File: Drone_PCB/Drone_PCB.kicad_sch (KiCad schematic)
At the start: 13 parts, among them U1 STM32F411RCT6

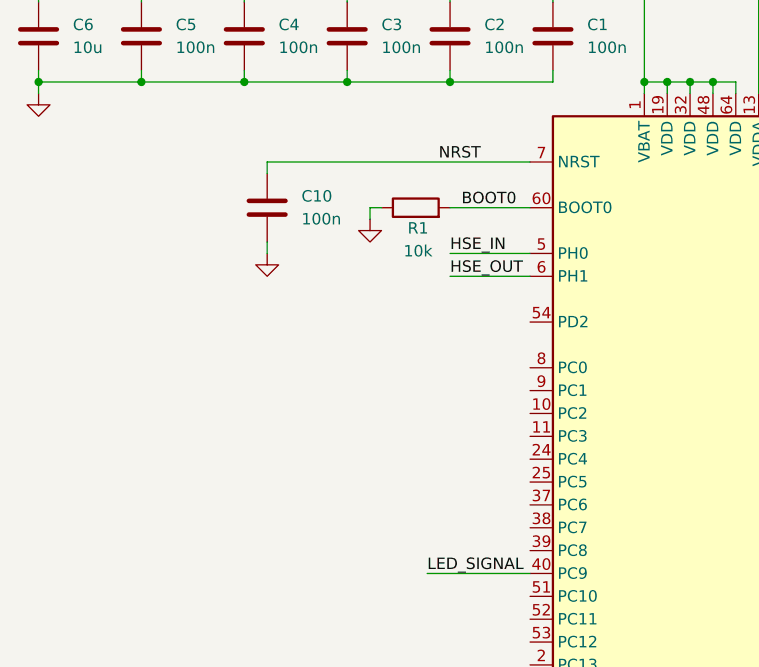
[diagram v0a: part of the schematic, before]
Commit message: Crystal Oscillator
I've decided to pick this one:
https://www.tme.eu/pl/details/26.00m-smdhc49s/rezonatory-kwarcowe-smd/yic/
It has 26MHz ( it's maximum input from STM Cube IDE ). It has 20pF, so to calculate two other capacitors we do this: 20pF - 5pF (that's maximum constant value)
15pF * 2 = 30pF each
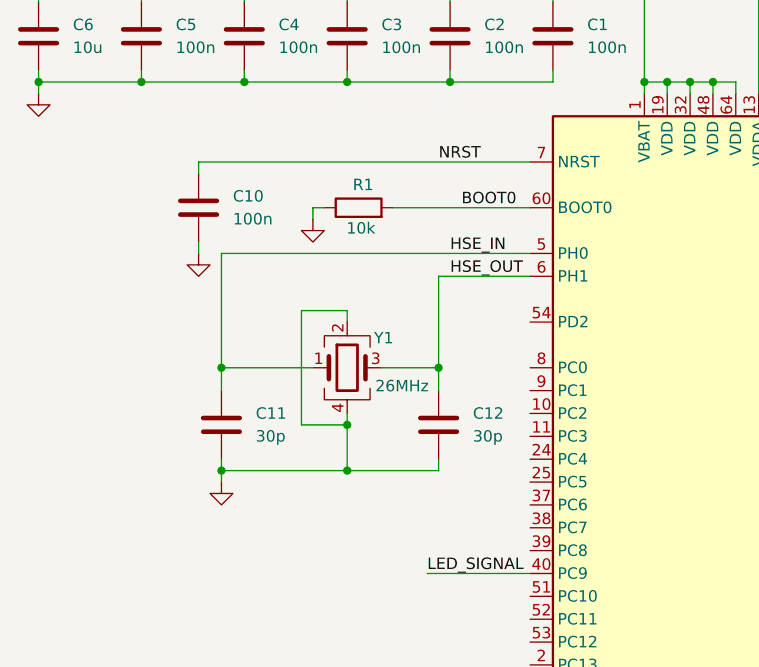
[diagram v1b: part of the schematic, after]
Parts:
- added C11, C12: 30p, symbol Device:C
- added Y1: 26MHz, symbol Device:Crystal_GND24
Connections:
- net GND: now also C11.2, C12.2, Y1.2, Y1.4
- net HSE_IN: now also C11.1, Y1.1
- net HSE_OUT: now also C12.1, Y1.3
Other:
- moved on the sheet: C10, R1

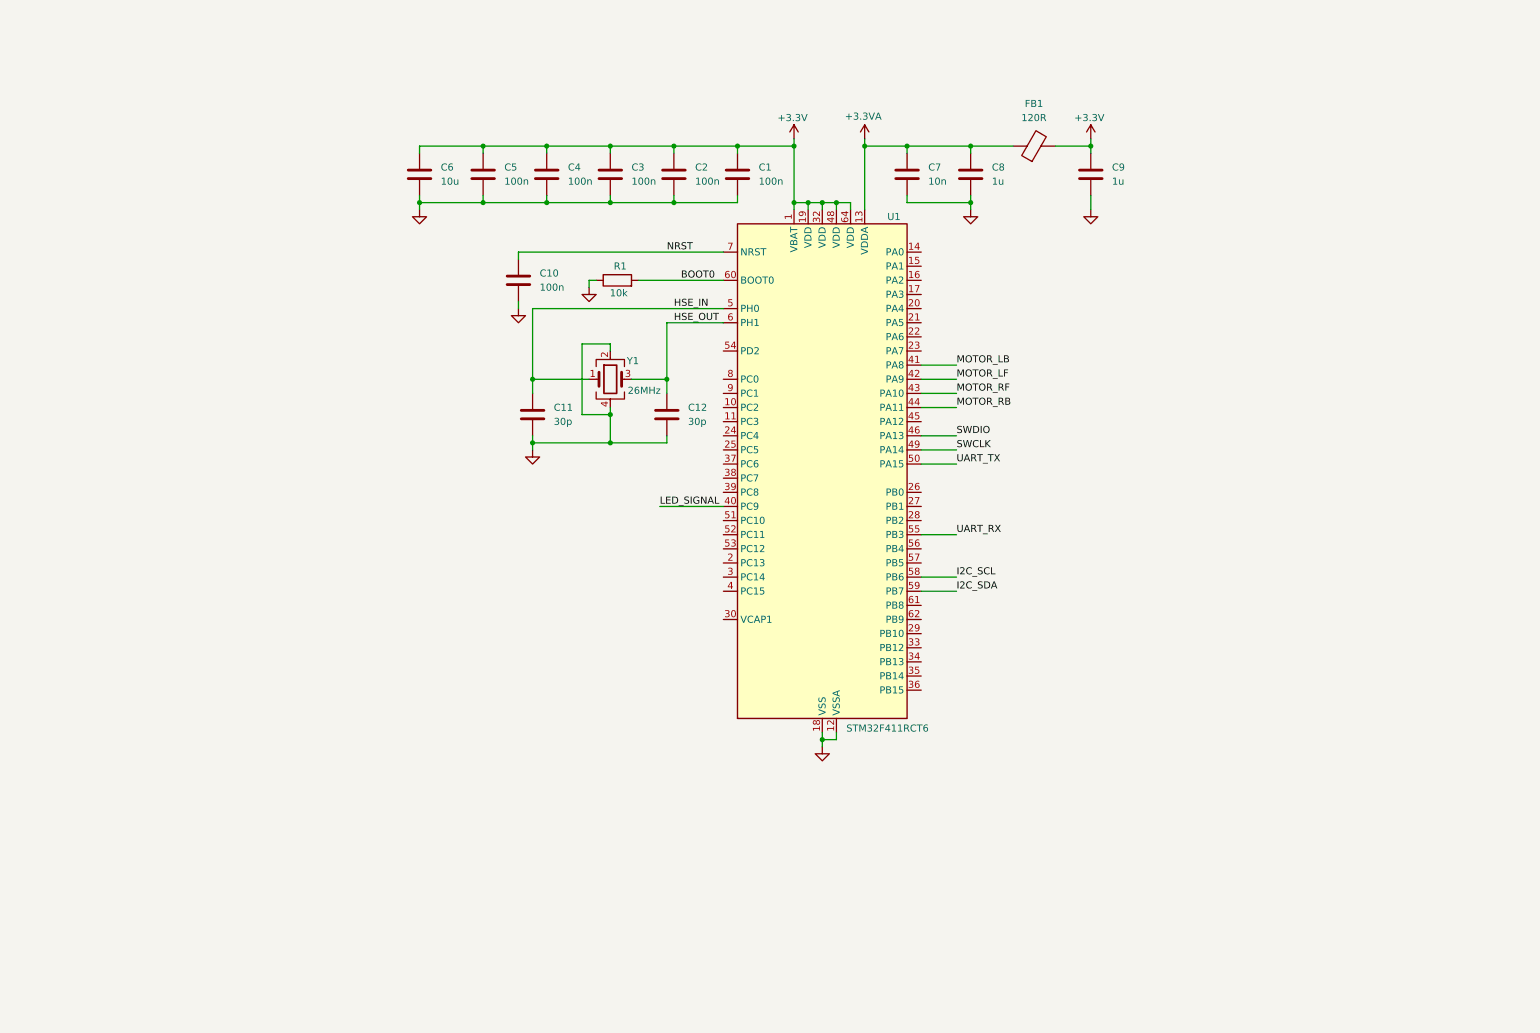
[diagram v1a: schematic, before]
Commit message: Voltage regulator + Outputs
I selected AP2112K as voltage regulator from 5/3.7V to 3.3V.
https://www.tme.eu/pl/details/ap2112k-3.3trg1/stabilizatory-napiecia-nieregulowane-ldo/diodes-incorporated/
In future I will add charging module
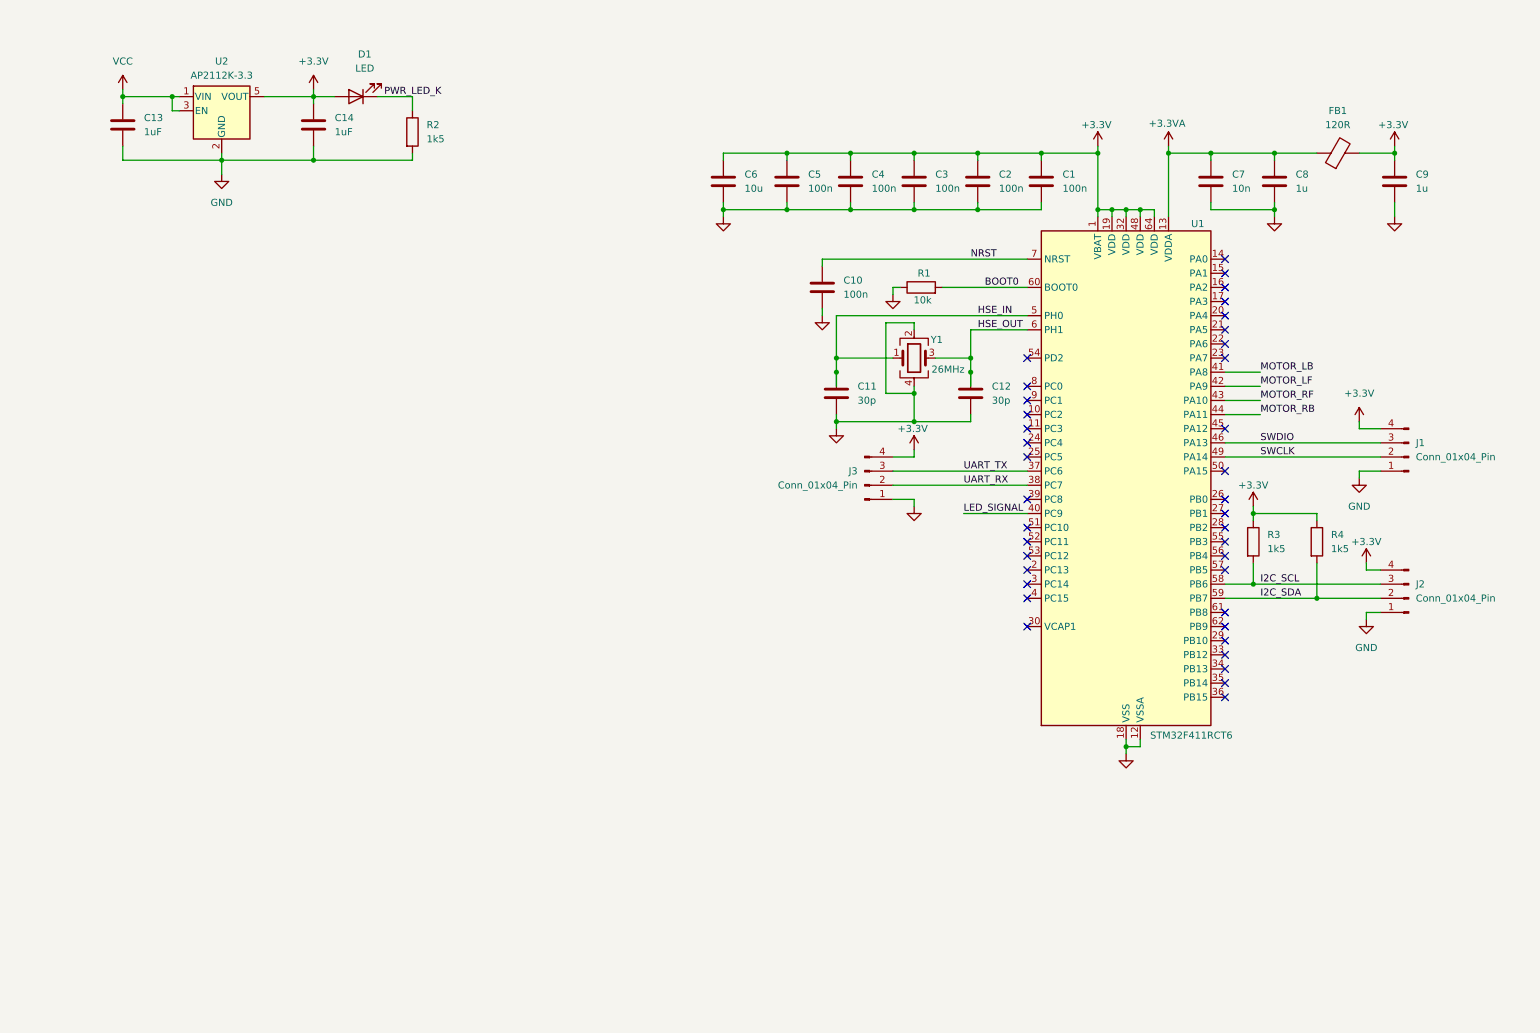
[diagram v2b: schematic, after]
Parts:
- added C13, C14: 1uF, symbol Device:C
- added D1: LED, symbol Device:LED
- added J1, J2, J3: Conn_01x04_Pin, symbol Connector:Conn_01x04_Pin
- added R2, R3, R4: 1k5, symbol Device:R
- added U2: AP2112K-3.3, Package_TO_SOT_SMD:SOT-23-5, symbol Regulator_Linear:AP2112K-3.3
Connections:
- net +3.3V: now also C14.1, D1.2 (A), J1.4 (Pin_4), J2.4 (Pin_4), J3.4 (Pin_4), R3.1, R4.1, U2.5 (VOUT)
- net GND: now also C13.2, C14.2, J1.1 (Pin_1), J2.1 (Pin_1), J3.1 (Pin_1), R2.2, U2.2 (GND)
- net I2C_SCL: now also J2.3 (Pin_3), R3.2
- net I2C_SDA: now also J2.2 (Pin_2), R4.2
- net SWCLK: now also J1.2 (Pin_2)
- net SWDIO: now also J1.3 (Pin_3)
- net UART_RX: now also U1.38 (PC7), J3.2 (Pin_2); no longer U1.55 (PB3)
- net UART_TX: now also U1.37 (PC6), J3.3 (Pin_3); no longer U1.50 (PA15)
- new net PWR_LED_K: D1.1 (K), R2.1
- new net VCC: C13.1, U2.1 (VIN), U2.3 (EN)
- no-connect marks 0 -> 38
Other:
- moved on the sheet: C1, C10, C11, C12, C2, C3, C4, C5, C6, C7, C8, C9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

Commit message: Notes and other output
Added outputs for LED_SIGNAL, MOTORs and proper connection of SWD. Also added schmatic notes
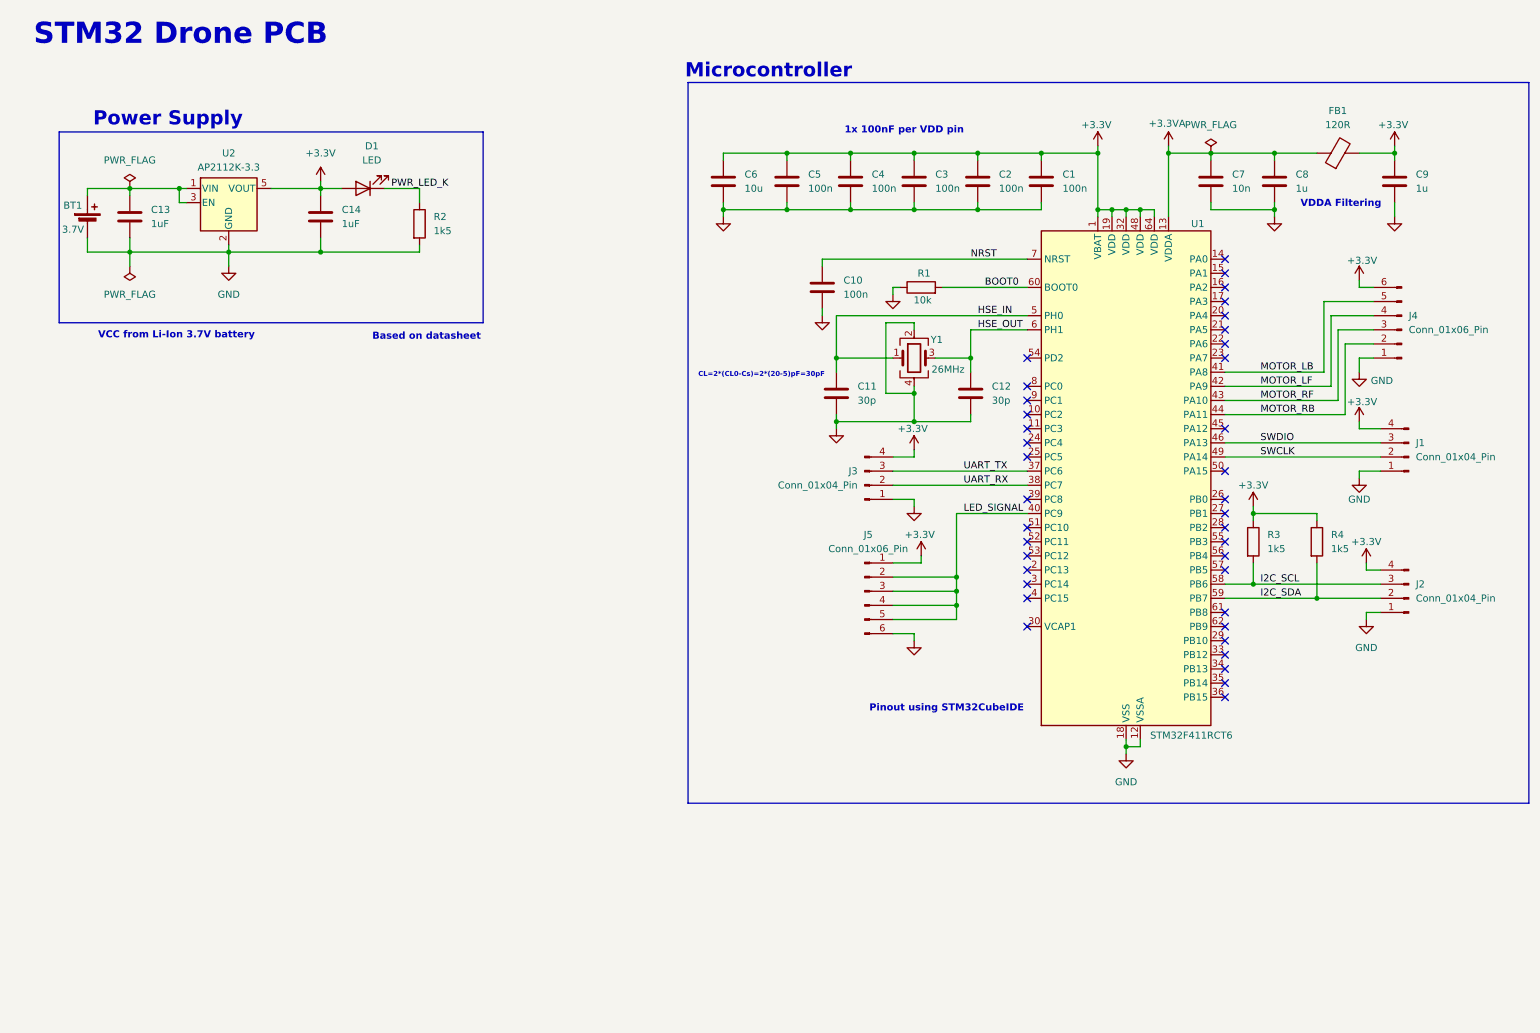
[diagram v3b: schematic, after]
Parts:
- added BT1: 3.7V, symbol Device:Battery_Cell
- added J4, J5: Conn_01x06_Pin, symbol Connector:Conn_01x06_Pin
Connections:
- net +3.3V: now also J4.6 (Pin_6), J5.1 (Pin_1)
- net GND: now also BT1.2 (-), J4.1 (Pin_1), J5.6 (Pin_6)
- net LED_SIGNAL: now also J5.2 (Pin_2), J5.3 (Pin_3), J5.4 (Pin_4), J5.5 (Pin_5)
- net MOTOR_LB: now also J4.5 (Pin_5)
- net MOTOR_LF: now also J4.4 (Pin_4)
- net MOTOR_RB: now also J4.2 (Pin_2)
- net MOTOR_RF: now also J4.3 (Pin_3)
- net VCC: no longer names the net of C13.1, U2.1 (VIN), U2.3 (EN)
- net VCC: now also BT1.1 (+)
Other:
- note added: "1x 100nF per VDD pin"
- note added: "Based on datasheet"
- note added: "CL=2*(CL0-Cs)=2*(20-5)pF=30pF"
- note added: "Microcontroller"
- note added: "Pinout using STM32CubeIDE"
- note added: "Power Supply"
- note added: "STM32 Drone PCB"
- note added: "VCC from Li-Ion 3.7V battery"
- note added: "VDDA Filtering"
- company: (none) -> Mateusz Jankowski
- title: (none) -> STM32 Drone PCB
- moved on the sheet: C13, C14, D1, R2, U2
